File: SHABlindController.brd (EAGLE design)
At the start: 98 x 30 mm, 34 parts, among them IC1 SPARKCORE, IC2 RAC02-3.3SC, IC3 MOC3042S, IC4 MOC3042S, IC5 RXB1SIL, T1 MOC3042M, T2 MOC3042M

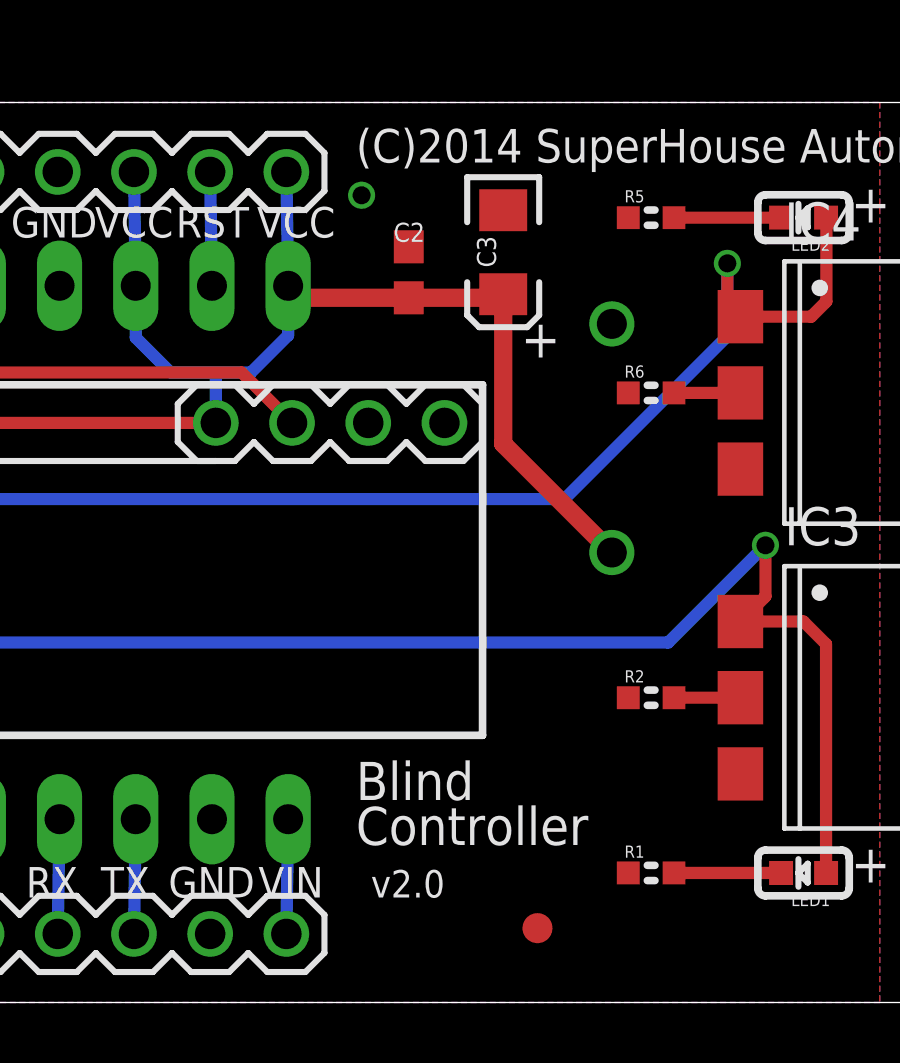
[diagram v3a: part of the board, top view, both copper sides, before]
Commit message: Changed power supply from 3.3V to 5V
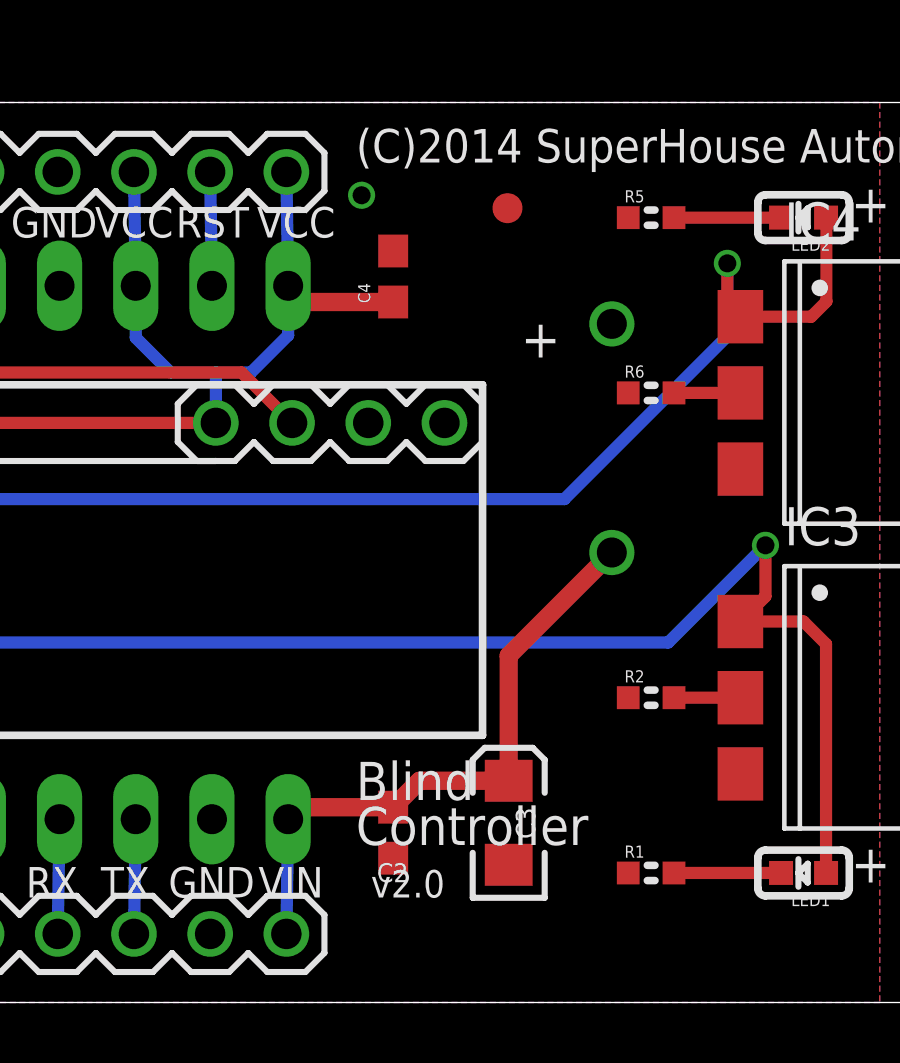
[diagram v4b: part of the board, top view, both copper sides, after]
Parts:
- added C4: 1uF 0603, freetronics:0603@1
- IC2: value RAC02-3.3SC -> RAC02-05SC
- moved FID3 24.0 mm to (46.6, 26.5)
- moved C3 19.0 mm to (46.6, 5.99), turned to 90 degrees
- moved C2 18.7 mm to (42.7, 5.66), turned to 270 degrees
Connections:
- net GND: now also C4.2
- net VCC: now also C4.1; no longer C2.1, C3.A, IC2.4
- net VIN: now also C2.1, C3.A, IC2.4
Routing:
- net VIN: track 3.82 -> 20.7 mm
- net VCC: track 61.6 -> 48.4 mm
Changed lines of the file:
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@@
 <setting verticaltext="up"/>
 </settings>
-<grid distance="0.5" unitdist="mm" unit="mm" style="dots" multiple="1" display="yes" altdistance="0.001" altunitdist="inch" altunit="inch"/>
+<grid distance="1" unitdist="mm" unit="mm" style="dots" multiple="1" display="yes" altdistance="0.001" altunitdist="inch" altunit="inch"/>
 <layers>
 <layer number="1" name="Top" color="4" fill="1" visible="yes" active="yes"/>
@@
 <circle x="90.328" y="27.654" radius="1.016" width="1.016" layer="41"/>
 <circle x="14.587" y="13.112" radius="1.016" width="1.016" layer="41"/>
-<circle x="47.551" y="2.478" radius="1.016" width="1.016" layer="41"/>
+<circle x="46.551" y="26.478" radius="1.016" width="1.016" layer="41"/>
 <hole x="95" y="3" drill="2.8"/>
 <hole x="95" y="27" drill="2.8"/>
@@
 <element name="FID1" library="freetronics" package="FIDUCIAL-1X2.5" value="FIDUCIAL1X2.5" x="90.328" y="27.654" smashed="yes"/>
 <element name="FID2" library="freetronics" package="FIDUCIAL-1X2.5" value="FIDUCIAL1X2.5" x="14.587" y="13.112" smashed="yes"/>
-<element name="C3" library="freetronics" package="EIA3216" value="10uF 6.3V A TANT" x="46.408" y="25.01" smashed="yes" rot="R270">
-<attribute name="NAME" x="46.17" y="24.502" size="0.635" layer="25" ratio="17" rot="R90"/>
-<attribute name="VALUE" x="46.898" y="24.74" size="0.635" layer="27" ratio="17"/>
-</element>
-<element name="C2" library="freetronics" package="0603@1" value="1uF 0603" x="43.26" y="24.34" smashed="yes" rot="R90">
-<attribute name="NAME" x="42.752" y="25.356" size="0.635" layer="25" font="vector" ratio="17"/>
-<attribute name="VALUE" x="43.903" y="26.324" size="1.016" layer="27" font="vector" ratio="17" rot="R90"/>
-</element>
-<element name="FID3" library="freetronics" package="FIDUCIAL-1X2.5" value="FIDUCIAL1X2.5" x="47.551" y="2.478" smashed="yes"/>
+<element name="C3" library="freetronics" package="EIA3216" value="10uF 6.3V A TANT" x="46.592" y="5.99" smashed="yes" rot="R90">
+<attribute name="NAME" x="46.83" y="6.498" size="0.635" layer="25" ratio="17" rot="R270"/>
+<attribute name="VALUE" x="46.102" y="6.26" size="0.635" layer="27" ratio="17" rot="R180"/>
+</element>
+<element name="C2" library="freetronics" package="0603@1" value="1uF 0603" x="42.74" y="5.66" smashed="yes" rot="R270">
+<attribute name="NAME" x="43.248" y="4.644" size="0.635" layer="25" font="vector" ratio="17" rot="R180"/>
+<attribute name="VALUE" x="42.097" y="3.676" size="1.016" layer="27" font="vector" ratio="17" rot="R270"/>
+</element>
+<element name="FID3" library="freetronics" package="FIDUCIAL-1X2.5" value="FIDUCIAL1X2.5" x="46.551" y="26.478" smashed="yes"/>
 <element name="T1" library="freetronics-original" package="SOT223" value="MOC3042M" x="81.93" y="11.43" smashed="yes" rot="R90">
 <attribute name="NAME" x="77.4215" y="10.6045" size="0.4064" layer="25" rot="R90"/>
@@
 <element name="JP8" library="freetronics-original" package="1X12" value="M12PTH" x="11.24" y="2.286"/>
 <element name="JP9" library="freetronics-original" package="1X12" value="M12PTH" x="11.24" y="27.686"/>
-<element name="IC2" library="freetronics-jon" package="RAC0X-SC" value="RAC02-3.3SC" x="64" y="15" rot="MR0"/>
+<element name="IC2" library="freetronics-jon" package="RAC0X-SC" value="RAC02-05SC" x="64" y="15" rot="MR0"/>
+<element name="C4" library="freetronics" package="0603@1" value="1uF 0603" x="42.74" y="24.2" rot="R90"/>
 </elements>
 <signals>
@@
 <contactref element="JP9" pad="9"/>
 <contactref element="IC2" pad="3"/>
+<contactref element="C4" pad="2"/>
 </signal>
 <signal name="N$10">
 </signal>
 <signal name="VCC" class="1">
-<contactref element="C3" pad="A"/>
 <contactref element="IC1" pad="P$10"/>
 <contactref element="IC1" pad="P$12"/>
@@
 <wire x1="34.16" y1="22.16" x2="35.32" y2="21" width="0.4064" layer="16"/>
 <wire x1="35.32" y1="21" x2="36.83" y2="21" width="0.4064" layer="16"/>
-<contactref element="C2" pad="1"/>
-<contactref element="IC2" pad="4"/>
 <wire x1="36.83" y1="21" x2="38" y2="21" width="0.4064" layer="16"/>
 <wire x1="36.83" y1="19.32" x2="36.83" y2="21" width="0.4064" layer="16"/>
-<wire x1="43.26" y1="23.49" x2="39.64" y2="23.49" width="0.6096" layer="1"/>
 <wire x1="39.64" y1="23.49" x2="39.24" y2="23.89" width="0.6096" layer="1"/>
-<wire x1="43.26" y1="23.49" x2="46.288" y2="23.49" width="0.6096" layer="1"/>
-<wire x1="46.288" y1="23.49" x2="46.408" y2="23.61" width="0.6096" layer="1"/>
-<wire x1="50.03" y1="15" x2="46.408" y2="18.622" width="0.6096" layer="1"/>
-<wire x1="46.408" y1="18.622" x2="46.408" y2="23.61" width="0.6096" layer="1"/>
+<contactref element="C4" pad="1"/>
+<wire x1="42.74" y1="23.35" x2="39.78" y2="23.35" width="0.6096" layer="1"/>
+<wire x1="39.78" y1="23.35" x2="39.24" y2="23.89" width="0.6096" layer="1"/>
 </signal>
 <signal name="NEUTRAL">
@@
 <contactref element="IC1" pad="P$13"/>
 <wire x1="39.24" y1="6.11" x2="39.18" y2="2.286" width="0.4064" layer="16"/>
+<contactref element="C3" pad="A"/>
+<contactref element="C2" pad="1"/>
+<contactref element="IC2" pad="4"/>
+<wire x1="42.74" y1="6.51" x2="39.64" y2="6.51" width="0.6096" layer="1"/>
+<wire x1="39.64" y1="6.51" x2="39.24" y2="6.11" width="0.6096" layer="1"/>
+<wire x1="42.74" y1="6.51" x2="43.62" y2="7.39" width="0.6096" layer="1"/>
+<wire x1="43.62" y1="7.39" x2="46.592" y2="7.39" width="0.6096" layer="1"/>
+<wire x1="46.592" y1="7.39" x2="46.592" y2="11.562" width="0.6096" layer="1"/>
+<wire x1="46.592" y1="11.562" x2="50.03" y2="15" width="0.6096" layer="1"/>
 </signal>
 <signal name="D3">

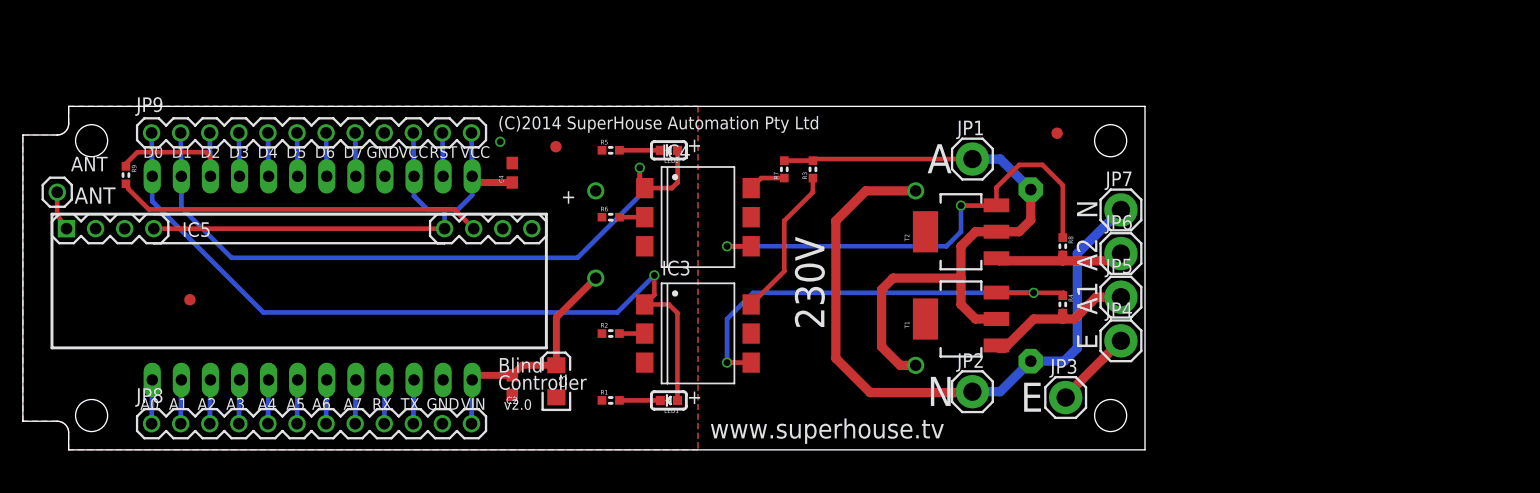
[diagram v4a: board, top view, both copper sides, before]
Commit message: Replaced TRIACs with relays; changed power supply to 5V; added piezo
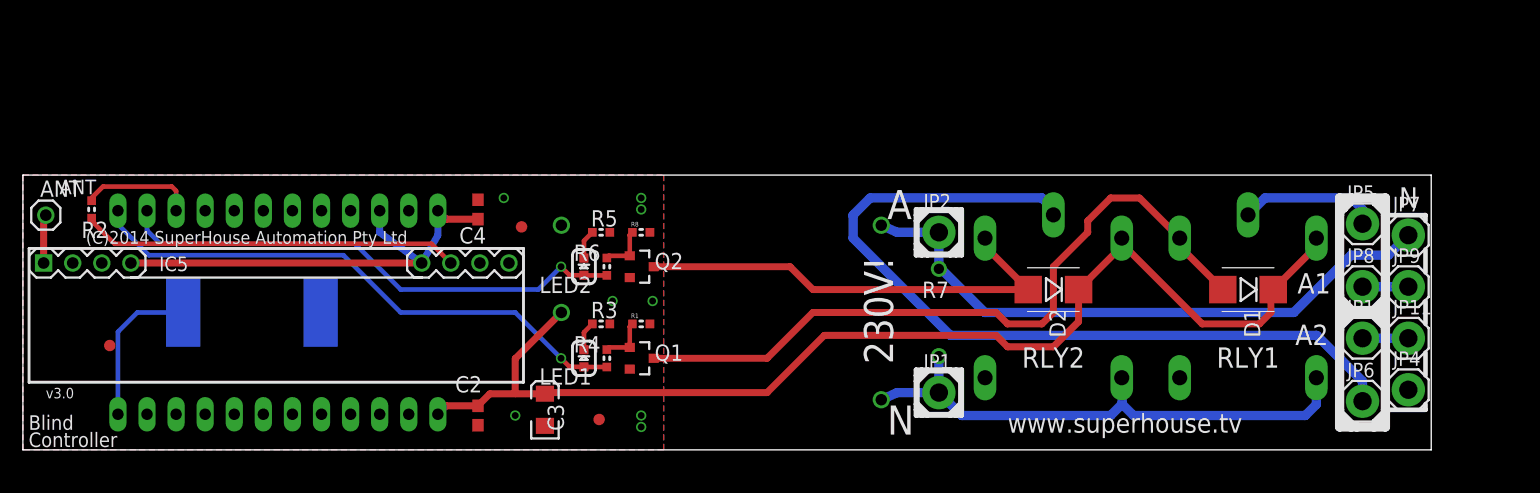
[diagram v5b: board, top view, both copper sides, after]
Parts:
- removed C1: 0.33uF 275V, capacitor-wima:C15B9
- removed IC3, IC4: MOC3042S, freetronics-jon:DIL6-SMD
- removed JP3: EARTH, freetronics-master-v1.1:1X01LARGE
- removed R9: 1K, freetronics:0603
- removed T1, T2: MOC3042M, freetronics-original:SOT223
- added D1, D2: 1N4004, freetronics-master-v1.1:SMB-DIODE
- added JP10, JP11: ACTIVE2, freetronics-master-v1.1:1X01LARGE
- added PIEZO: BUZZERSMD12X12, freetronics-master-v1:BUZZER-12X12-SMT
- added Q1, Q2: 2N7002, freetronics-master-v1:SOT23-3
- added RLY1, RLY2: G5L, relay:G5LE
- JP8, JP9: value M12PTH -> ACTIVE1; device freetronics-original:1X12 -> freetronics-master-v1.1:1X01LARGE
- R1, R8: value 330R -> 10K
- R2, R4, R6: value 330R -> 1K
- R3: value 56R -> 330R
- R7: value 56R -> VARISTOR 423V 2.5KA; device freetronics:0603 -> freetronics-master-v1.1:AXIAL-0.3
- moved JP9 110.6 mm to (121.0, 14.2)
- moved JP8 106.4 mm to (117.0, 14.2)
- moved FID1 47.2 mm to (50.3, 2.65)
- moved R2 46.6 mm to (6.00, 21.0), turned to 270 degrees
- moved R4 40.1 mm to (51.0, 8.00)
- moved R8 36.8 mm to (54.0, 19.0), turned to 0 degrees
- moved JP4 25.5 mm to (121.0, 5.25)
- moved JP7 25.2 mm to (121.0, 18.8)
- moved JP6 24.7 mm to (117.0, 4.25)
- moved R3 22.9 mm to (50.5, 11.0), turned to 180 degrees
- moved JP5 22.1 mm to (117.0, 19.8)
- moved JP1 20.6 mm to (80.0, 5.00)
- moved R7 18.4 mm to (80.0, 12.0), flipped to the bottom, turned to 270 degrees
- moved JP2 14.2 mm to (80.0, 19.0)
- moved LED2 12.6 mm to (49.0, 16.0), turned to 0 degrees
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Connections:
- removed net N$12: IC3.4, R4.1, T1.3
- removed net N$13: IC3.6, R3.1
- removed net N$15: JP3.1, JP4.1
- removed net N$16: IC4.4, R8.1, T2.3
- removed net N$18: IC3.2, R2.2
- removed net N$20: IC4.6, R7.1
- new net EARTH: JP4.1
- new net N$3: D2.A, Q2.3, RLY2.2
- new net N$5: Q1.1, R1.1, R4.1
- new net N$6: Q2.1, R6.1, R8.1
- new net N$7: JP8.1, JP9.1
- new net N$8: JP10.1, JP11.1
- net A0: now also PIEZO.1; no longer JP8.1
- net A1: no longer JP8.2
- net A2: no longer JP8.3
- net A3: no longer JP8.4
- net A4: no longer JP8.5
- net A5: no longer JP8.6
- net A6: no longer JP8.7
- net A7: no longer JP8.8
- net ACTIVE: now also R7.P$2, RLY1.S, RLY2.S; no longer C1.1, R3.2, R7.2, T1.2, T2.2
- net D0: now also R4.2; no longer IC3.1, JP9.1
- net D1: now also R6.2; no longer IC4.1, JP9.2
- net D2: now also R2.1; no longer JP9.3, R9.1
- net D3: no longer JP9.4
- net D4: no longer JP9.5
- net D5: no longer JP9.6
- net D6: no longer JP9.7
- net D7: no longer JP9.8
- net GND: now also PIEZO.2, Q1.2, Q2.2, R1.2, R3.1, R8.2; no longer JP8.11, JP9.9, R1.1, R2.1, R6.1
- net N$135: now also R2.2; no longer R9.2
- net N$14: now also RLY1.P; no longer R4.2, T1.1
- net N$17: now also RLY2.P; no longer R8.2, T2.1
- net N$25: now also R3.2; no longer R1.2
- net N$4: now also D1.A, Q1.3, RLY1.2; no longer IC4.2, R6.2
- net NEUTRAL: now also R7.P$1; no longer C1.2
- net RST: no longer JP9.11
- net RX: no longer JP8.9
- net TX: no longer JP8.10
- net VCC: no longer JP9.10, JP9.12
- net VIN: now also D1.C, D2.C, RLY1.1, RLY2.1; no longer JP8.12
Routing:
- net VIN: track 20.7 -> 102.7 mm
- net N$4: track 2.21 -> 63.0 mm
- net N$17: track 11.7 -> 72.4 mm
- net N$16: track 41.9 -> 0.00 mm, vias 2 -> 0
- net N$12: track 39.9 -> 0.00 mm, vias 2 -> 0
- net N$3: track 0.00 -> 39.6 mm
- net D0: track 68.9 -> 49.1 mm
- net D1: track 60.9 -> 45.2 mm
- net N$13: track 13.3 -> 0.00 mm
- net A0: track 3.82 -> 13.6 mm
- net ACTIVE: track 57.2 -> 48.0 mm
- net VCC: track 48.4 -> 40.6 mm
- net N$15: track 6.95 -> 0.00 mm
- net N$6: track 0.00 -> 4.23 mm
- net N$5: track 0.00 -> 4.23 mm
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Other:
- board size 98 x 30 mm -> 123 x 24 mm
- board text added: "230V!"
- board text added: "v3.0"
- board text removed: "+"
- board text removed: "230V"
- board text removed: "A0"
- board text removed: "A3"
- board text removed: "A4"
- board text removed: "A5"
- board text removed: "A6"
- board text removed: "A7"
- board text removed: "D0"
- board text removed: "D1"
- board text removed: "D2"
- board text removed: "D3"
- board text removed: "D4"
- board text removed: "D5"
- board text removed: "D6"
- board text removed: "D7"
- board text removed: "E"
- board text removed: "GND"
- board text removed: "RST"
- board text removed: "RX"
- board text removed: "TX"
- board text removed: "VCC"
- board text removed: "VIN"
- board text removed: "v2.0"

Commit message: Release v3.0
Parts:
- removed C4: 1uF 0603, freetronics:0603@1
- removed JP11: ACTIVE2, freetronics-master-v1.1:1X01LARGE
- added C1: 1uF 0603, freetronics:0603@1
- added JP3: ACTIVE1, freetronics-master-v1.1:1X01LARGE
- C2: value 1uF 0603 -> 10uF 6.3V A TANT; device freetronics:0603@1 -> freetronics:EIA3216
- C3: value 10uF 6.3V A TANT -> 1uF 0603; device freetronics:EIA3216 -> freetronics:0603@1
- JP10: value ACTIVE2 -> EARTH
- JP4: value EARTH -> ACTIVE1
- JP5, JP9: value ACTIVE1 -> ACTIVE2
- moved C3 18.5 mm to (39.7, 21.0)
- moved JP4 15.0 mm to (117.0, 19.8)
- moved JP5 10.0 mm to (117.0, 9.75)
- moved JP10 6.02 mm to (121.0, 5.25)
- moved C2 5.87 mm to (45.6, 3.50), turned to 90 degrees
- moved JP9 4.50 mm to (121.0, 9.75)
- moved JP8 4.00 mm to (121.0, 14.2)
- renumbered IC5 to IC3
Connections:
- net EARTH: now also JP10.1; no longer JP4.1
- net GND: now also C1.2, C2.C, C3.2; no longer C2.2, C3.C, C4.2
- net N$14: now also JP4.1; no longer JP5.1
- net N$7: now also JP3.1; no longer JP9.1
- net N$8: now also JP5.1, JP9.1; no longer JP10.1, JP11.1
- net VCC: now also C3.1; no longer C4.1
- net VIN: now also C1.1, C2.A; no longer C2.1, C3.A
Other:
- board text added: "2 x 330R 0603 3 x 1K 0603 2 x 10K 0603 2 x 1N4004 SMA 2 x 1uF 0603 1 x 10uF 6.3V TANT 2 x 2N7002 2 x GREEN LED"
